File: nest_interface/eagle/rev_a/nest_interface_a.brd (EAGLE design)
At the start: 133.3 x 110.5 mm, 114 parts, among them J1 MOLEX_MICRO_USB_B_047346, J10 CONN_BLOCK_2, J11 CONN_BLOCK_2, J12 CONN_BLOCK_2, J13 CONN_BLOCK_2, J14 CONN_BLOCK_3, J15 CONN_BLOCK_3, J16 CONN_BLOCK_7, J17 CONN_BLOCK_7, J18 CONN_BLOCK_8, J19 CONN_BLOCK_8, J2 MOLEX_MICRO_USB_B_047346, J20 CONN_BLOCK_8, J21 CONN_BLOCK_8, J5 PJ-036A-SMT, J6 CONN_BLOCK_2, J7 CONN_BLOCK_2, J8 CONN_BLOCK_2, J9 CONN_BLOCK_2, U1 EPIC-CORE_A, U2 MSP430F1611IPM, U3 FT232RL, U4 FT232RL, U5 MPC1825, U6 TC1262, U7 PCA9575, U8 PCA9575, Y1 FC-135_32.768KA-A3

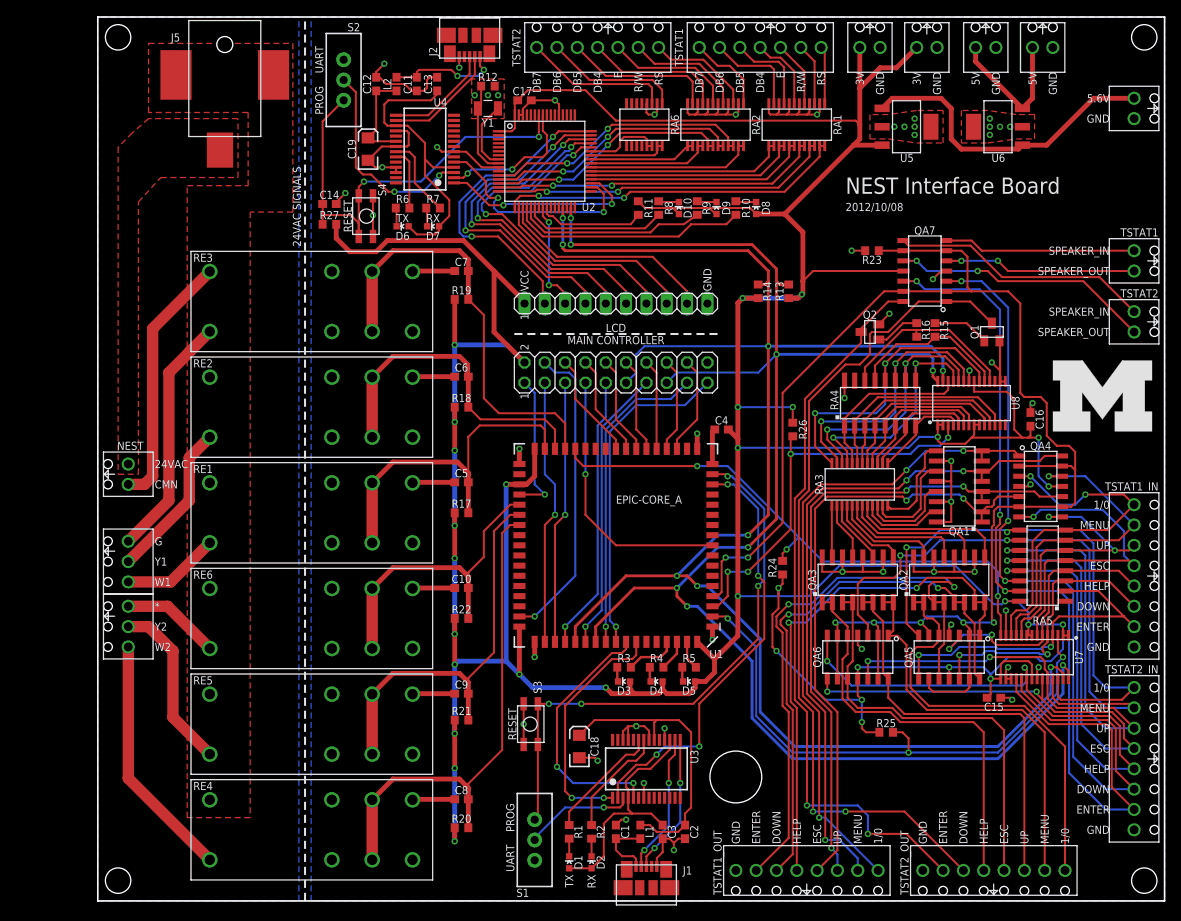
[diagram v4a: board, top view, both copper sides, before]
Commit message: board changes, lcd code
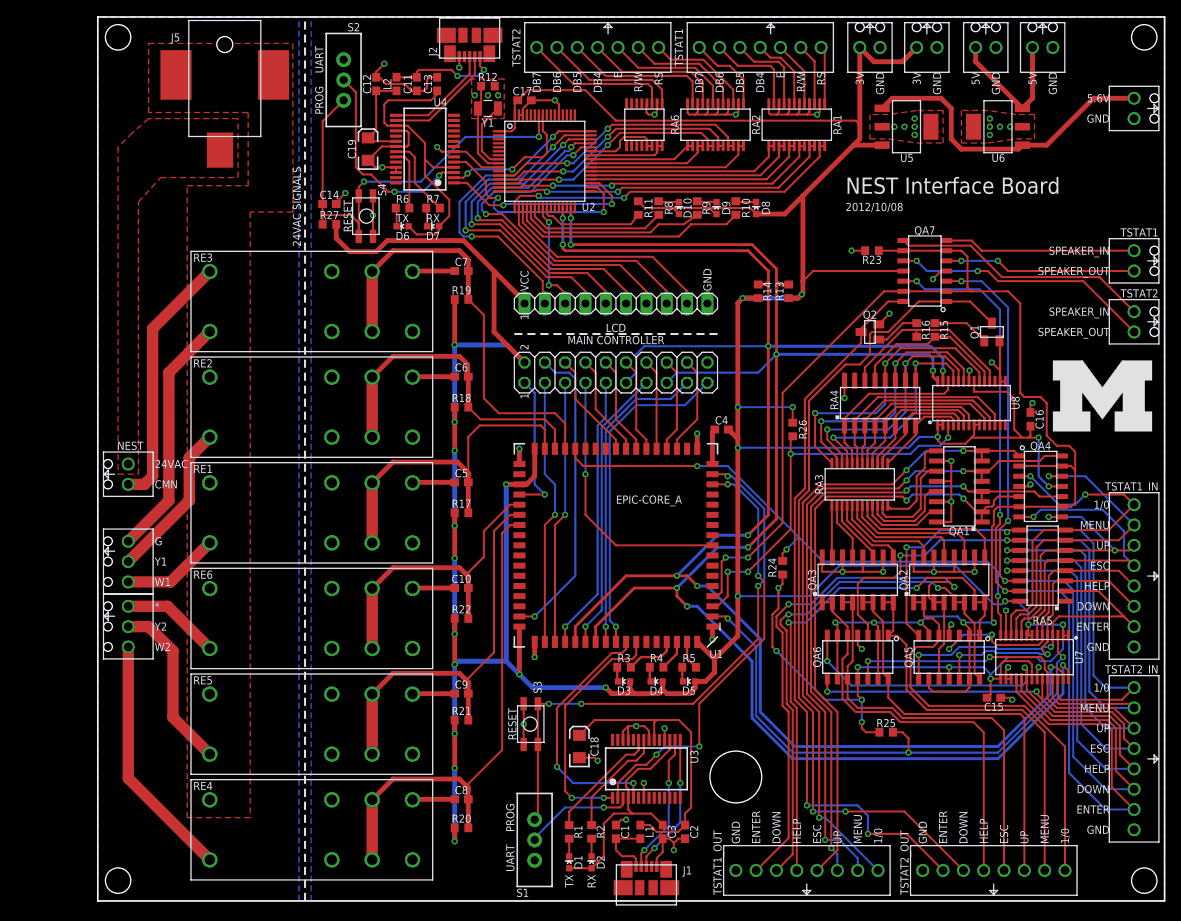
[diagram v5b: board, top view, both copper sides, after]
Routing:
- net VCC: track 607.6 -> 608.3 mm
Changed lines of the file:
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@@
 <?xml version="1.0" encoding="utf-8"?>
 <!DOCTYPE eagle SYSTEM "eagle.dtd">
-<eagle version="6.2">
+<eagle version="6.3">
 <drawing>
 <settings>
@@
 </class>
 </classes>
-<designrules>
+<designrules name="default">
 <description language="en">&lt;b&gt;EAGLE Design Rules for *2* Layer Designs (DS)&lt;/b&gt;
 &lt;p&gt;
@@
 <wire x1="88.011" y1="75.819" x2="88.138" y2="75.946" width="0.6096" layer="1"/>
 <wire x1="88.138" y1="75.946" x2="88.138" y2="77.47" width="0.6096" layer="1"/>
-<wire x1="88.138" y1="77.47" x2="88.138" y2="83.59" width="0.6096" layer="1"/>
-<wire x1="88.138" y1="83.59" x2="85.864" y2="85.864" width="0.6096" layer="1"/>
+<wire x1="88.138" y1="77.47" x2="88.138" y2="88.138" width="0.6096" layer="1"/>
 <wire x1="82.55" y1="75.35" x2="80.606" y2="75.35" width="0.6096" layer="1"/>
 <via x="80.606" y="75.35" extent="1-16" drill="0.4064" diameter="0.4064"/>
@@
 <wire x1="96.012" y1="21.082" x2="95.504" y2="21.59" width="0.254" layer="1"/>
 <wire x1="95.25" y1="95.25" x2="95.25" y2="97.028" width="0.6096" layer="1"/>
-<wire x1="95.25" y1="97.028" x2="95.25" y2="101.6" width="0.6096" layer="1"/>
-<wire x1="95.25" y1="101.6" x2="95.25" y2="106.68" width="0.6096" layer="1"/>
-<wire x1="102.362" y1="106.68" x2="99.822" y2="104.14" width="0.6096" layer="1"/>
-<wire x1="99.822" y1="104.14" x2="97.79" y2="104.14" width="0.6096" layer="1"/>
-<wire x1="97.79" y1="104.14" x2="95.25" y2="101.6" width="0.6096" layer="1"/>
-<wire x1="85.864" y1="85.864" x2="94.474" y2="94.474" width="0.6096" layer="1"/>
+<wire x1="95.25" y1="97.028" x2="95.25" y2="106.68" width="0.6096" layer="1"/>
+<wire x1="85.864" y1="85.864" x2="88.138" y2="88.138" width="0.6096" layer="1"/>
+<wire x1="88.138" y1="88.138" x2="94.474" y2="94.474" width="0.6096" layer="1"/>
 <wire x1="94.474" y1="94.474" x2="98.042" y2="94.474" width="0.6096" layer="1"/>
 <wire x1="94.474" y1="94.474" x2="95.25" y2="95.25" width="0.6096" layer="1"/>
@@
 <contactref element="JP1" pad="1"/>
 <wire x1="53.34" y1="74.93" x2="53.34" y2="74.676" width="0.6096" layer="1"/>
+<wire x1="102.362" y1="106.68" x2="100.584" y2="104.902" width="0.6096" layer="1"/>
+<wire x1="100.584" y1="104.902" x2="97.028" y2="104.902" width="0.6096" layer="1"/>
+<wire x1="97.028" y1="104.902" x2="95.25" y2="106.68" width="0.6096" layer="1"/>
 </signal>
 <signal name="GND">

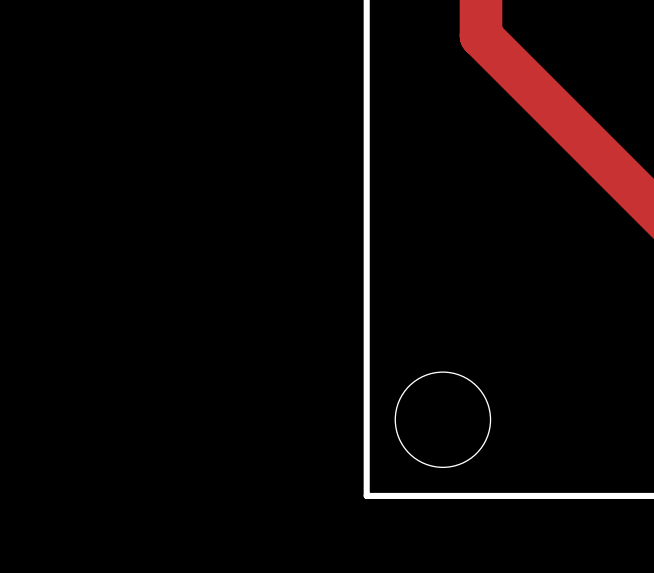
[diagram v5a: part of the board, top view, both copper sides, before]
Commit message: nib: before big keypad control change
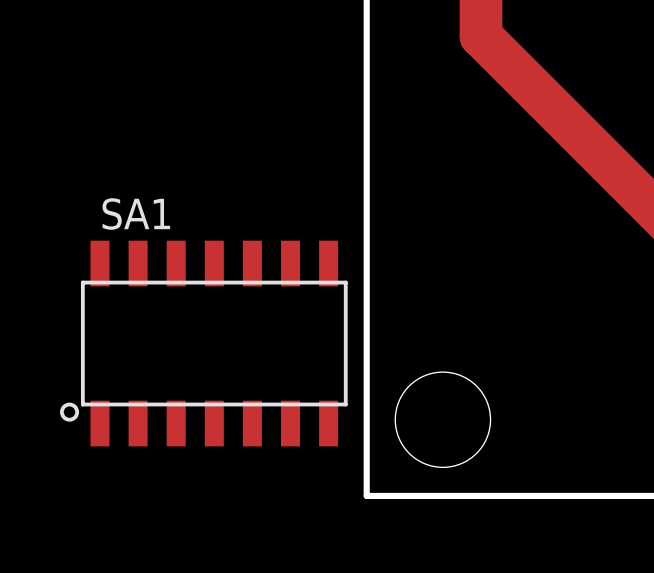
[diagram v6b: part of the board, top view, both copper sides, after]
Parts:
- added SA1: TS12A44515DR, nest_interface:SOIC-14
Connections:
- new net N$42: SA1.4
- new net N$59: SA1.9
- new net N$61: SA1.10
- new net N$62: SA1.1
- new net N$63: SA1.3
- new net N$64: SA1.8
- new net N$66: SA1.11
- new net N$67: SA1.14
- new net N$68: SA1.7
- net #KEYPAD_ENABLE: now also SA1.12, SA1.13, SA1.5, SA1.6
- net TSTAT1_ON/OFF_OUT_PIN: now also SA1.2
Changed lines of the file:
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@@
 </element>
 <element name="U$1" library="nest_interface" package="UMICH_SOLID_350MIL" value="UMICH_SOLID_LARGE" x="119.38" y="58.674"/>
+<element name="SA1" library="nest_interface" package="SOIC-14" value="TS12A44515DR" x="-5.08" y="5.08">
+<attribute name="DIGIKEY" value="296-24790-1-ND" x="-5.08" y="5.08" size="1.778" layer="27" display="off"/>
+</element>
 </elements>
 <signals>
@@
 <wire x1="118.618" y1="62.23" x2="117.856" y2="62.992" width="0.254" layer="1"/>
 <wire x1="117.856" y1="62.992" x2="115.824" y2="62.992" width="0.254" layer="1"/>
+<contactref element="SA1" pad="13"/>
+<contactref element="SA1" pad="5"/>
+<contactref element="SA1" pad="12"/>
+<contactref element="SA1" pad="6"/>
+<wire x1="-2.54" y1="2.413" x2="76.835" y2="38.1" width="0" layer="19" extent="1-1"/>
+<wire x1="-3.81" y1="2.413" x2="-2.54" y2="2.413" width="0" layer="19" extent="1-1"/>
+<wire x1="-6.35" y1="7.747" x2="-3.81" y2="2.413" width="0" layer="19" extent="1-1"/>
+<wire x1="-7.62" y1="7.747" x2="-6.35" y2="7.747" width="0" layer="19" extent="1-1"/>
 </signal>
 <signal name="TSTAT1_ON/OFF_IN">
@@
 <wire x1="98.7425" y1="54.737" x2="102.235" y2="58.2295" width="0.254" layer="1"/>
 <wire x1="102.235" y1="58.2295" x2="102.235" y2="59.436" width="0.254" layer="1"/>
+<contactref element="SA1" pad="2"/>
+<wire x1="-7.62" y1="2.413" x2="98.7425" y2="54.737" width="0" layer="19" extent="1-1"/>
 </signal>
 <signal name="TSTAT1_MENU_OUT_PIN">
@@
 <wire x1="102.362" y1="80.01" x2="100.711" y2="80.01" width="0.254" layer="1"/>
 </signal>
+<signal name="N$42">
+<contactref element="SA1" pad="4"/>
+</signal>
+<signal name="N$59">
+<contactref element="SA1" pad="9"/>
+</signal>
+<signal name="N$61">
+<contactref element="SA1" pad="10"/>
+</signal>
+<signal name="N$62">
+<contactref element="SA1" pad="1"/>
+</signal>
+<signal name="N$63">
+<contactref element="SA1" pad="3"/>
+</signal>
+<signal name="N$64">
+<contactref element="SA1" pad="8"/>
+</signal>
+<signal name="N$66">
+<contactref element="SA1" pad="11"/>
+</signal>
+<signal name="N$67">
+<contactref element="SA1" pad="14"/>
+</signal>
+<signal name="N$68">
+<contactref element="SA1" pad="7"/>
+</signal>
 </signals>

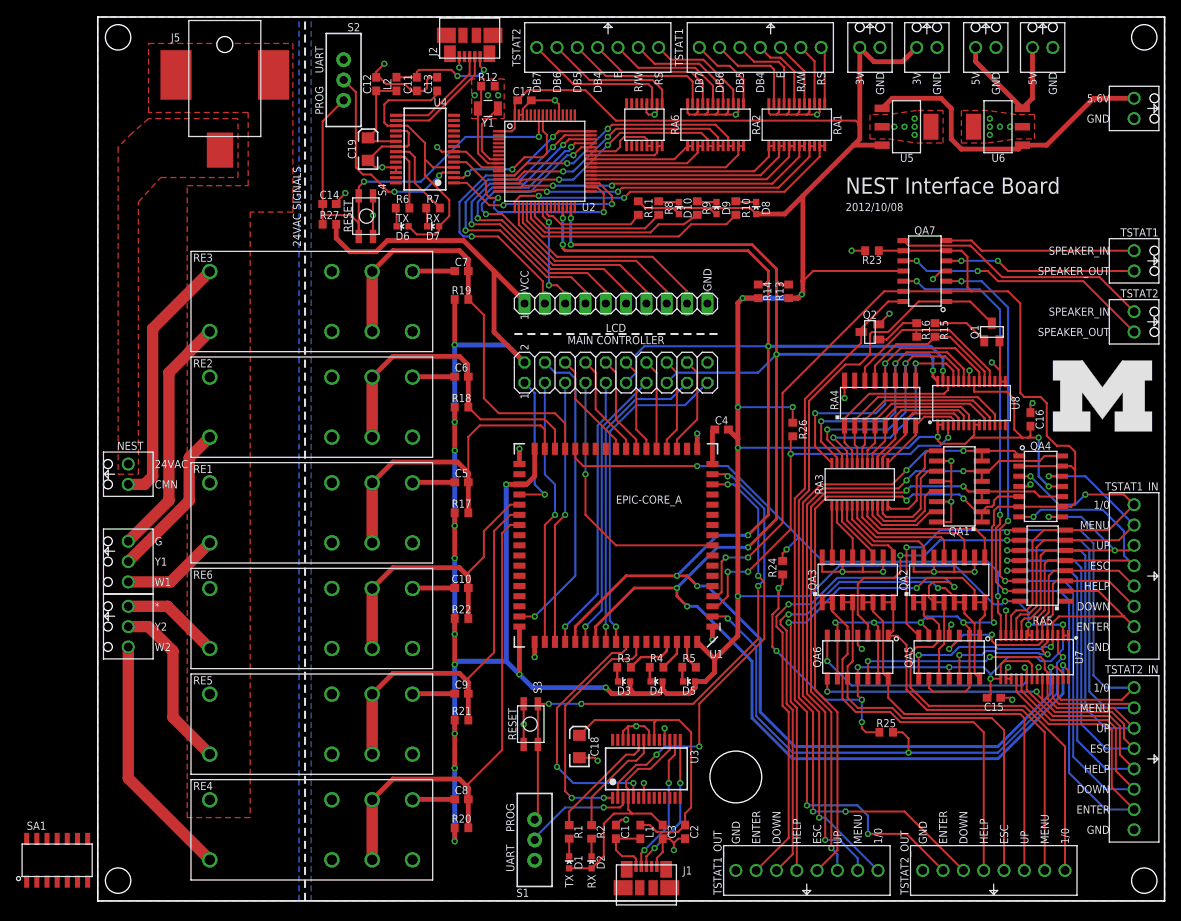
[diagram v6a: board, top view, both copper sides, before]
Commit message: new ciruict routed - no airwires
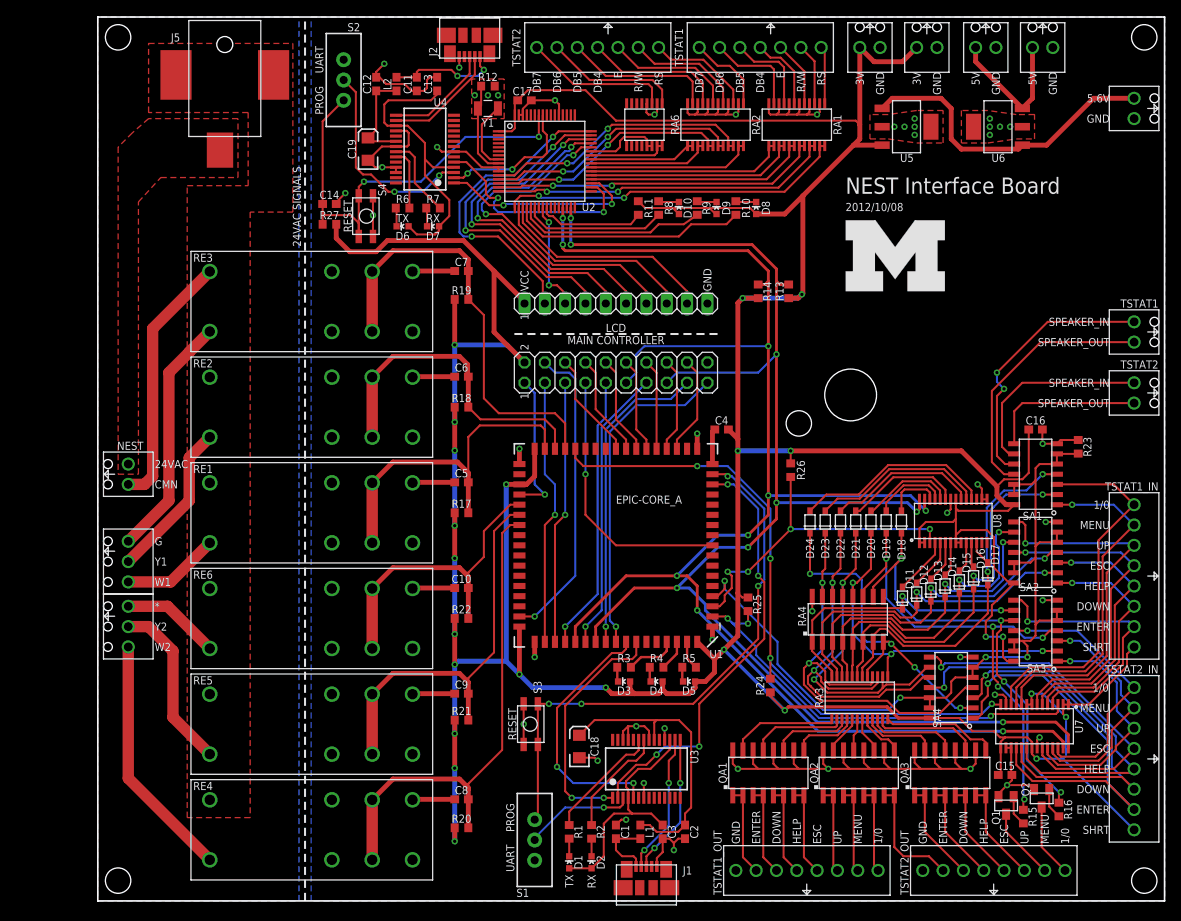
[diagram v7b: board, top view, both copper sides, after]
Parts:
- removed QA4, QA5, QA6, QA7: ALD1107, nest_interface:SOIC-14
- removed RA5: 766161104GP, nest_interface:SOIC-16
- added D11, D12, D13, D14, D15, D16, D17, D18, D19, D20, D21, D22, D23, D24: B5818WS-SCHOTTKY-DIODE, nest_interface:SOD-323
- added SA2, SA3, SA4: TS12A44515DR, nest_interface:SOIC-14
- moved SA1 131.5 mm to (117.2, 53.3), turned to 90 degrees
- moved R16 62.5 mm to (120.1, 11.4), turned to 90 degrees
- moved Q2 62.1 mm to (118.0, 12.8), turned to 180 degrees
- moved R15 61.8 mm to (115.7, 10.5), turned to 90 degrees
- moved Q1 59.2 mm to (113.5, 11.9), turned to 180 degrees
- moved QA1 43.0 mm to (83.8, 16.0), turned to 90 degrees
- moved R23 35.6 mm to (122.6, 56.8), turned to 90 degrees
- moved U$1 31.3 mm to (93.5, 76.2)
- moved RA4 27.3 mm to (93.8, 35.2)
- moved QA3 26.8 mm to (106.6, 16.0)
- moved RA3 26.7 mm to (95.2, 25.4)
- moved QA2 26.6 mm to (95.1, 16.0)
- moved R25 23.5 mm to (81.3, 37.1), turned to 270 degrees
- moved U8 14.9 mm to (106.9, 47.5)
- moved R24 14.8 mm to (84.1, 26.9)
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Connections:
- removed net N$16 (its old number): QA1.11, RA3.23
- removed net N$37 (its old number): QA1.9, RA3.24
- removed net N$42: SA1.4
- removed net N$58 (its old number): QA1.13, RA3.22
- removed net N$59: SA1.9
- removed net N$60: QA1.15, RA3.21
- removed net N$61: SA1.10
- removed net N$62: SA1.1
- removed net N$63: SA1.3
- removed net N$64: SA1.8
- removed net N$65: QA3.9, RA3.16
- removed net N$66: SA1.11
- removed net N$67: SA1.14
- removed net N$68: SA1.7
- new net N$17: QA1.13, RA3.14
- new net N$25: QA1.11, RA3.15
- new net N$26: QA1.9, RA3.16
- new net N$27: QA3.9, RA3.24
- new net N$33: QA1.15, RA3.13
- new net TSTAT1_DOWN_OUT_CTRL: D12.P$2, RA3.11, RA4.2, SA2.2
- new net TSTAT1_ENTER_OUT_CTRL: D11.P$2, RA3.12, RA4.1, SA3.9
- new net TSTAT1_ESC_OUT_CTRL: D14.P$2, RA3.9, RA4.4, SA2.10
- new net TSTAT1_HELP_OUT_CTRL: D13.P$2, RA3.10, RA4.3, SA2.4
- new net TSTAT1_MENU_OUT_CTRL: D16.P$2, RA3.7, RA4.6, SA1.2
- new net TSTAT1_ON/OFF_OUT_CTRL: D17.P$2, RA3.6, RA4.7, SA1.4
- new net TSTAT1_UP_OUT_CTRL: D15.P$2, RA3.8, RA4.5, SA2.9
- new net TSTAT2_DOWN_OUT_CTRL: D23.P$2, RA3.4, RA4.15, SA4.4
- new net TSTAT2_ENTER_OUT_CTRL: D24.P$2, RA3.5, RA4.8, SA4.2
- new net TSTAT2_ESC_OUT_CTRL: D21.P$2, RA3.2, RA4.13, SA4.9
- new net TSTAT2_HELP_OUT_CTRL: D22.P$2, RA3.3, RA4.14, SA4.10
- new net TSTAT2_MENU_OUT_CTRL: D19.P$2, R15.2, RA4.11, SA3.4
- new net TSTAT2_ON/OFF_OUT_CTRL: D18.P$2, R16.2, RA4.10, SA3.10
- new net TSTAT2_UP_OUT_CTRL: D20.P$2, RA3.1, RA4.12, SA3.2
- net #KEYPAD_ENABLE: now also SA2.12, SA2.13, SA2.5, SA2.6, SA3.12, SA3.13, SA3.5, SA3.6, SA4.12, SA4.13, SA4.5, SA4.6; no longer QA4.13, QA4.2, QA4.6, QA4.9, QA5.13, QA5.2, QA5.6, QA5.9, QA6.13, QA6.2, QA6.6, QA6.9, QA7.13, QA7.2, QA7.6, QA7.9
- net GND: now also SA1.7, SA2.7, SA3.7, SA4.7; no longer J18.1, J19.1, QA4.4, QA5.4, QA6.4, QA7.4
- net N$28: now also RA3.21; no longer RA3.13
- net N$29: now also RA3.22; no longer RA3.14
- net N$30: now also RA3.23; no longer RA3.15
- net TSTAT1_DOWN_IN: now also SA2.1; no longer QA5.12, RA5.3
- net TSTAT1_DOWN_OUT: now also QA1.3, QA1.4; no longer QA2.5, QA2.6, QA5.14
- net TSTAT1_DOWN_OUT_PIN: now also D12.P$1, U8.5; no longer RA3.6, RA4.3, U8.11
- net TSTAT1_ENTER_IN: now also SA3.8; no longer QA5.8, RA5.2
- net TSTAT1_ENTER_OUT: now also QA1.1, QA1.2; no longer QA2.3, QA2.4, QA5.10
- net TSTAT1_ENTER_OUT_PIN: now also D11.P$1, U8.4; no longer RA3.7, RA4.2, U8.12
- net TSTAT1_ESC_IN: now also SA2.11; no longer QA4.7, RA5.5
- net TSTAT1_ESC_OUT: now also QA1.7, QA1.8; no longer QA1.1, QA1.2, QA4.5
- net TSTAT1_ESC_OUT_PIN: now also D14.P$1; no longer RA3.4, RA4.5
- net TSTAT1_HELP_IN: now also SA2.3; no longer QA5.3, RA5.4
- net TSTAT1_HELP_OUT: now also QA1.5, QA1.6; no longer QA2.7, QA2.8, QA5.1
- net TSTAT1_HELP_OUT_PIN: now also D13.P$1, U8.6; no longer RA3.5, RA4.4, U8.10
- net TSTAT1_MENU_IN: now also SA1.1; no longer QA4.12, RA5.7
- net TSTAT1_MENU_OUT: now also QA2.3, QA2.4; no longer QA1.5, QA1.6, QA4.14
- net TSTAT1_MENU_OUT_PIN: now also D16.P$1, U8.11; no longer RA3.2, RA4.7, U8.5
- net TSTAT1_ON/OFF_IN: now also SA1.3; no longer QA4.3, RA5.8
- net TSTAT1_ON/OFF_OUT: now also QA2.5, QA2.6; no longer QA1.7, QA1.8, QA4.1
- net TSTAT1_ON/OFF_OUT_PIN: now also D17.P$1, U8.12; no longer RA3.1, RA4.8, SA1.2, U8.4
- net TSTAT1_SPEAKER_IN: now also SA1.10; no longer QA7.7
- net TSTAT1_SPEAKER_OUT: now also SA1.11; no longer QA7.5
- net TSTAT1_UP_IN: now also SA2.8; no longer QA4.8, RA5.6
- net TSTAT1_UP_OUT: now also QA2.1, QA2.2; no longer QA1.3, QA1.4, QA4.10
- net TSTAT1_UP_OUT_PIN: now also D15.P$1, U8.10; no longer RA3.3, RA4.6, U8.6
- net TSTAT2_DOWN_IN: now also SA4.3; no longer QA7.3, RA5.14
- net TSTAT2_DOWN_OUT: now also QA3.1, QA3.2; no longer Q1.3, QA7.1
- net TSTAT2_DOWN_OUT_PIN: now also D23.P$1; no longer R15.2, RA4.13
- net TSTAT2_ENTER_IN: now also SA4.1; no longer QA7.12, RA5.15
- net TSTAT2_ENTER_OUT: now also QA2.7, QA2.8; no longer Q2.3, QA7.14
- net TSTAT2_ENTER_OUT_PIN: now also D24.P$1; no longer R16.2, RA4.14
- net TSTAT2_ESC_IN: now also SA4.8; no longer QA6.8, RA5.12
- net TSTAT2_ESC_OUT: now also QA3.5, QA3.6; no longer QA3.3, QA3.4, QA6.10
- net TSTAT2_ESC_OUT_PIN: now also D21.P$1; no longer RA3.11, RA4.11
- net TSTAT2_HELP_IN: now also SA4.11; no longer QA6.7, RA5.13
- net TSTAT2_HELP_OUT: now also QA3.3, QA3.4; no longer QA3.1, QA3.2, QA6.5
- net TSTAT2_HELP_OUT_PIN: now also D22.P$1; no longer RA3.12, RA4.12
- net TSTAT2_MENU_IN: now also SA3.3; no longer QA6.3, RA5.10
- net TSTAT2_MENU_OUT: now also Q1.3; no longer QA3.7, QA3.8, QA6.1
- net TSTAT2_MENU_OUT_PIN: now also D19.P$1; no longer RA3.9, RA4.9
- net TSTAT2_ON/OFF_IN: now also SA3.11; no longer QA5.7, RA5.9
- net TSTAT2_ON/OFF_OUT: now also Q2.3; no longer QA2.1, QA2.2, QA5.5
- net TSTAT2_ON/OFF_OUT_PIN: now also D18.P$1; no longer RA3.8, RA4.1
- net TSTAT2_SPEAKER_IN: now also SA1.9; no longer QA7.8
- net TSTAT2_SPEAKER_OUT: now also SA1.8; no longer QA7.10
- net TSTAT2_UP_IN: now also SA3.1; no longer QA6.12, RA5.11
- net TSTAT2_UP_OUT: now also QA3.7, QA3.8; no longer QA3.5, QA3.6, QA6.14
- net TSTAT2_UP_OUT_PIN: now also D20.P$1; no longer RA3.10, RA4.10
- net VCC: now also J18.1, J19.1, SA1.14, SA2.14, SA3.14, SA4.14; no longer QA4.11, QA5.11, QA6.11, QA7.11, RA5.16
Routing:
- net TSTAT2_DOWN_OUT: track 105.0 -> 12.7 mm, vias 2 -> 0
- net #KEYPAD_ENABLE: track 196.2 -> 106.2 mm, vias 7 -> 4
- net TSTAT2_ENTER_OUT: track 92.1 -> 15.1 mm, vias 2 -> 0
- net TSTAT1_MENU_OUT: track 85.1 -> 10.9 mm, vias 3 -> 0
- net TSTAT1_ON/OFF_OUT: track 81.6 -> 10.9 mm, vias 3 -> 0
- net TSTAT1_UP_OUT: track 81.1 -> 10.9 mm, vias 3 -> 0
- net TSTAT1_ESC_OUT: track 77.4 -> 11.4 mm, vias 2 -> 0
- net TSTAT2_ENTER_IN: track 118.0 -> 53.5 mm, vias 3 -> 1
- net TSTAT1_ENTER_OUT: track 75.8 -> 11.4 mm, vias 2 -> 0
- net TSTAT2_MENU_OUT_CTRL: track 0.00 -> 62.6 mm, vias 0 -> 5
- net TSTAT2_DOWN_IN: track 108.8 -> 48.0 mm, vias 3 -> 1
- net TSTAT1_DOWN_OUT: track 69.4 -> 11.4 mm, vias 2 -> 0
- net TSTAT2_ON/OFF_OUT_CTRL: track 0.00 -> 57.4 mm, vias 0 -> 4
- net TSTAT2_DOWN_OUT_CTRL: track 0.00 -> 56.3 mm, vias 0 -> 2
- net TSTAT1_HELP_OUT: track 64.9 -> 11.4 mm, vias 2 -> 0
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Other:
- board text added: "SHRT"
